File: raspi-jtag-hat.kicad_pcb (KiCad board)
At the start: 2 copper layers, 65 x 56.5 mm, 8 parts, among them P1 FTDIUART, P2 RASPI, P3 JTAG, P4 PWRUTIL, P5 I2C

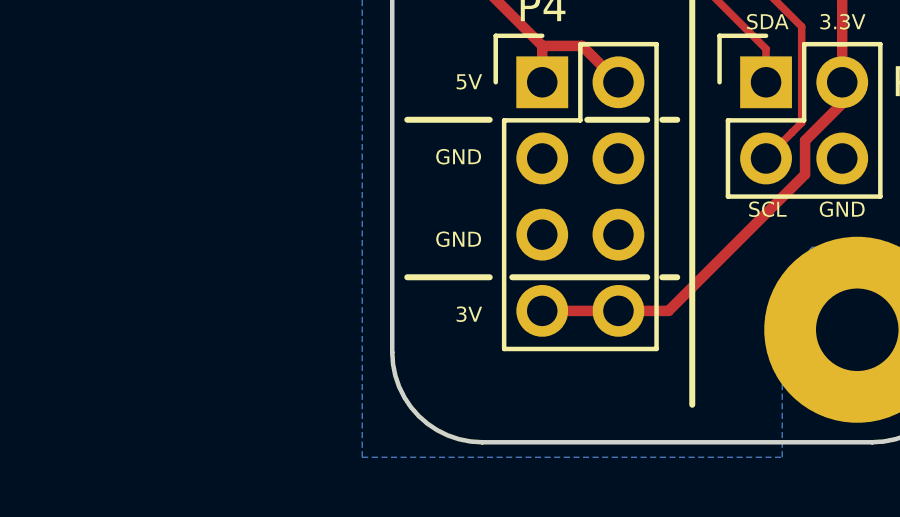
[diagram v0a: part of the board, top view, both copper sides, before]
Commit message: Change 3.3V header silkscreen caption to "3.3V"
Previously it said just "3V".
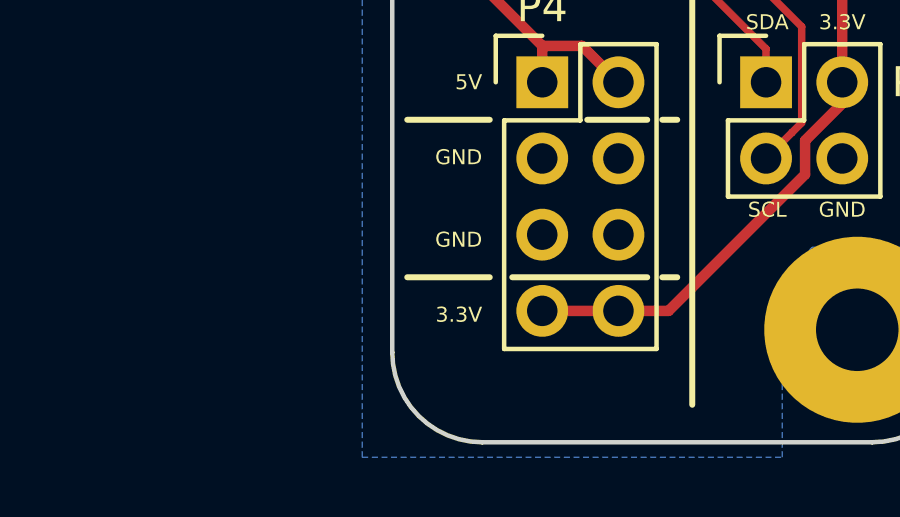
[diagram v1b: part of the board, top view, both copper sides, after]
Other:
- board text removed: "3V"
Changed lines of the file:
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@@
     (effects (font (size 0.5 0.5) (thickness 0.125)) (justify right))
   )
-  (gr_text 3V (at 49 52.25) (layer F.SilkS)
+  (gr_text 3.3V (at 49 52.25) (layer F.SilkS)
     (effects (font (size 0.5 0.5) (thickness 0.125)) (justify right))
   )

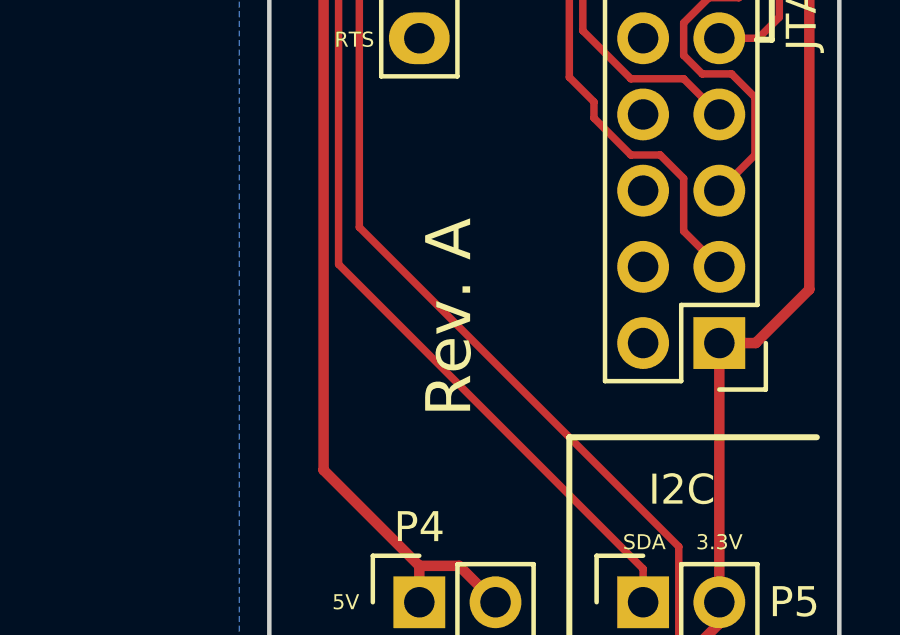
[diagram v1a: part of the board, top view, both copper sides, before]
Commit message: Update board silkscreen in preparation for Rev. B.
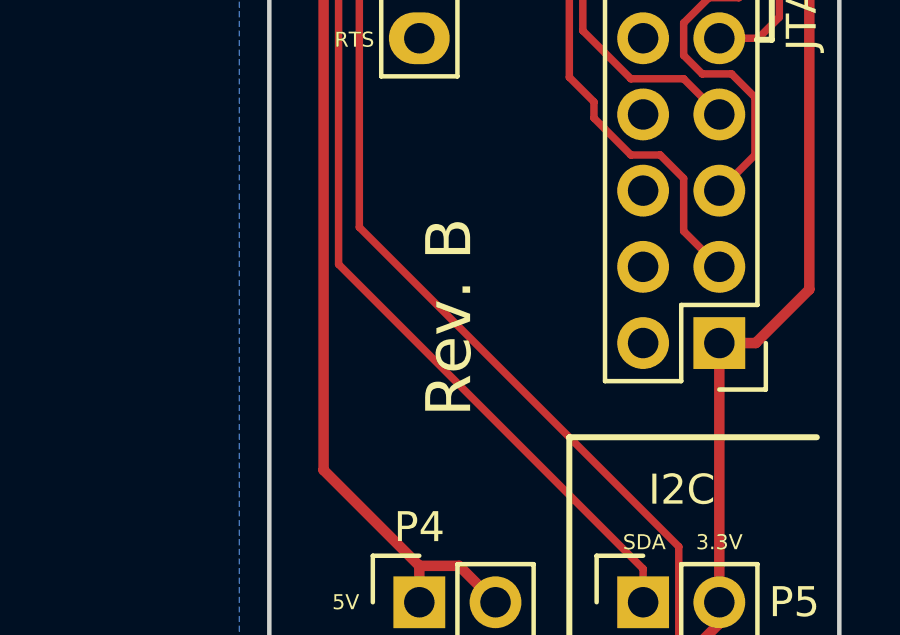
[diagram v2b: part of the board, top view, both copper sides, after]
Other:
- board text added: "Rev. B"
- board text removed: "Rev. A"
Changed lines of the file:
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@@
     (effects (font (size 0.5 0.5) (thickness 0.125)) (justify right))
   )
-  (gr_text "Rev. A" (at 52 35 90) (layer F.SilkS)
+  (gr_text "Rev. B" (at 52 35 90) (layer F.SilkS)
     (effects (font (size 1.5 1.5) (thickness 0.3)))
   )
